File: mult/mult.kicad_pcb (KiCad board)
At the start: 2 copper layers, 20 x 108 mm, 73 parts, among them J1 Eurorack_Mono_Jack, J10 Eurorack_Mono_Jack, J11 Eurorack_Mono_Jack_No_S, J12 Eurorack_Mono_Jack_No_S, J13 Eurorack_Mono_Jack, J14 Eurorack_Mono_Jack, J15 Eurorack_Mono_Jack_No_S, J16 Eurorack_Mono_Jack_No_S, J17 Eurorack_Power, J2 Eurorack_Mono_Jack, J3 Eurorack_Mono_Jack_No_S, J4 Eurorack_Mono_Jack_No_S, J5 Eurorack_Mono_Jack, J6 Eurorack_Mono_Jack, J7 Eurorack_Mono_Jack_No_S, J8 Eurorack_Mono_Jack_No_S, J9 Eurorack_Mono_Jack, U1 OPA1679, U2 OPA1679, U3 OPA1679, U4 OPA1679

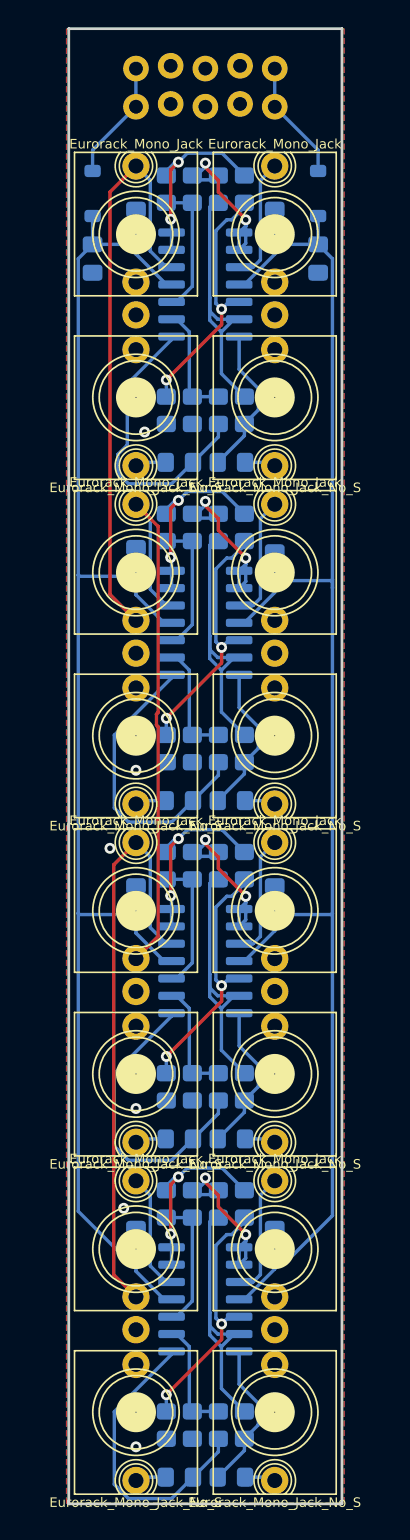
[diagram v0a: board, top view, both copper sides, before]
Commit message: mult: Reassign reference designators
This follows visual placement (left to right, top to bottom), except for
bulk capacitors which are enumerated left to right after bypass caps.
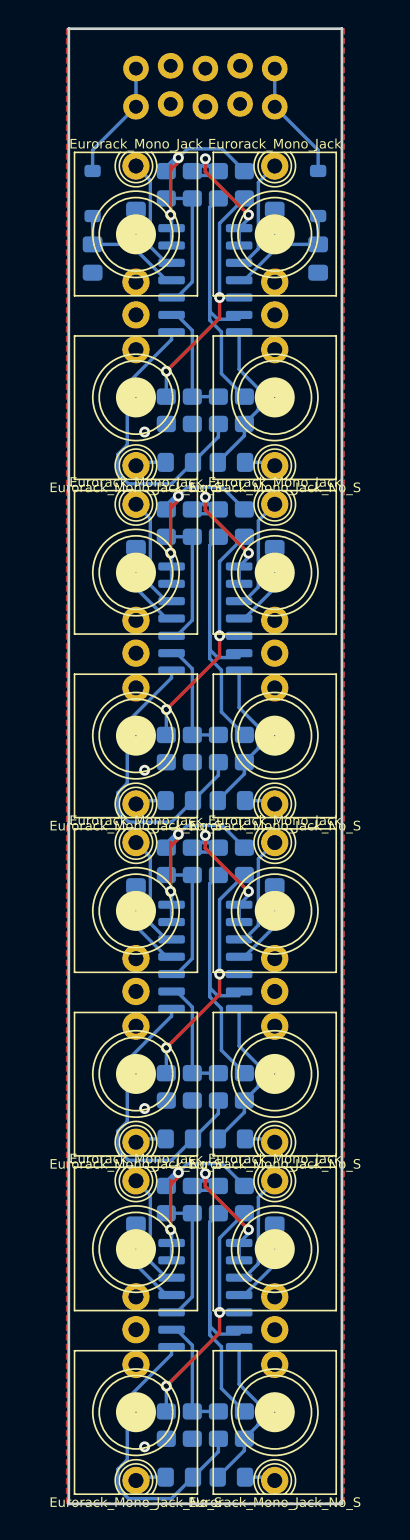
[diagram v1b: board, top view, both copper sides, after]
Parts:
- moved C7 0.32 mm to (15.2, 88.6)
- moved C8 0.32 mm to (5.08, 88.6)
- moved R31 0.32 mm to (13.0, 85.7)
- moved R32 0.32 mm to (11.1, 85.7)
- moved R33 0.32 mm to (9.21, 85.7)
- moved R34 0.32 mm to (7.30, 85.7)
- moved U3 0.32 mm to (10.2, 67.9)
- moved U4 0.32 mm to (10.2, 92.7)
- moved R11 0.32 mm to (13.0, 36.2)
- moved R12 0.32 mm to (11.1, 36.2)
- moved R13 0.32 mm to (9.21, 36.2)
- moved R14 0.32 mm to (7.30, 36.2)
- moved R21 0.32 mm to (13.0, 61.0)
- moved R22 0.32 mm to (11.1, 61.0)
- moved R23 0.32 mm to (9.21, 61.0)
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- renumbered C2 to C1, C9 to C10, C1 to C2, C4 to C3, C3 to C4, C6 to C5, C5 to C6, C8 to C7, C7 to C8, C10 to C9, D2 to D1, D1 to D2, R4 to R1, R5 to R10, R14 to R11, R13 to R12, R12 to R13, R11 to R14, R19 to R15, R17 to R16, R20 to R17, R16 to R19, R3 to R2, R15 to R20, R24 to R21, R23 to R22, R22 to R23, R21 to R24, R29 to R25, R27 to R26, R30 to R27, R26 to R29, R2 to R3, R25 to R30, R34 to R31, R33 to R32, R32 to R33, R31 to R34, R39 to R35, R37 to R36, R40 to R37, R36 to R39, R1 to R4, R35 to R40, R9 to R5, R7 to R6, R10 to R7, R6 to R9
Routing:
- net VEE: track 108.2 -> 21.5 mm
- net VCC: track 107.0 -> 21.5 mm
- net /channel 1/tip in (a): track 43.2 -> 8.01 mm
- net /channel 2/tip in (a): track 43.0 -> 8.01 mm
- net /channel 3/tip in (a): track 42.9 -> 8.01 mm
- net Net-(U2C--): track 14.4 -> 12.5 mm
- net Net-(U3C--): track 14.4 -> 12.5 mm
- net Net-(U1C--): track 14.4 -> 12.5 mm
- net Net-(U4C--): track 14.4 -> 12.5 mm
- net Net-(U4D--): track 20.5 -> 19.2 mm
- net Net-(U3D--): track 20.5 -> 19.2 mm
- net Net-(U1D--): track 20.5 -> 19.2 mm
- net Net-(U2D--): track 20.5 -> 19.2 mm
- net Net-(J10-Tip): track 9.08 -> 8.01 mm
- net Net-(J6-Tip): track 9.08 -> 8.01 mm
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
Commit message: mult: Add 0.5mm power traces
Not sure if this matters at all, but can't hurt.
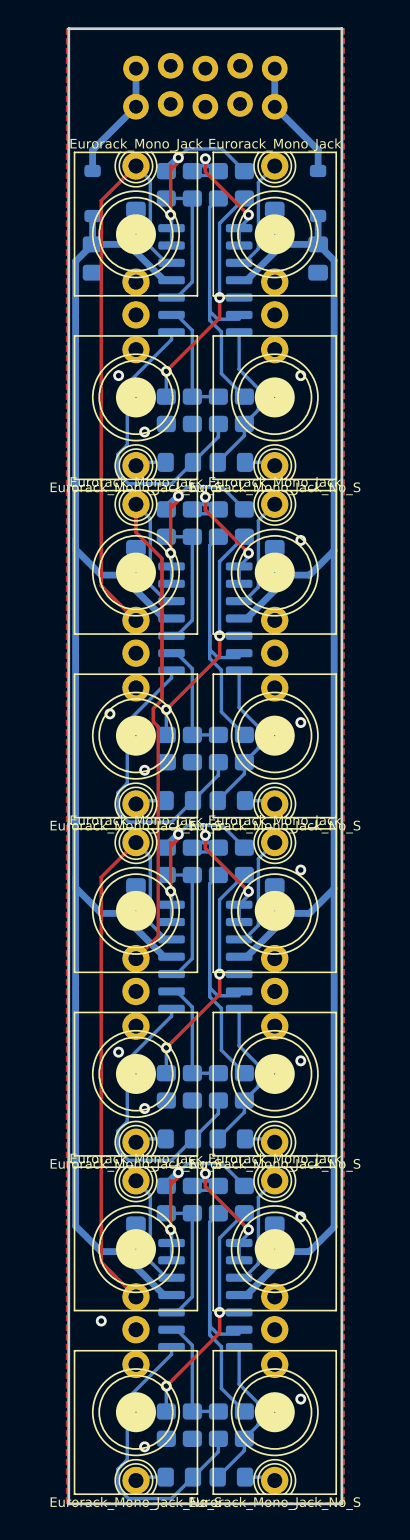
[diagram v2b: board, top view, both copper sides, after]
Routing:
- net VCC: track 21.5 -> 110.2 mm
- net VEE: track 21.5 -> 108.7 mm
- net /channel 3/tip in (a): track 8.01 -> 43.4 mm
- net /channel 1/tip in (a): track 8.01 -> 43.4 mm
- net /channel 2/tip in (a): track 8.01 -> 43.2 mm
- net GND: vias 4 -> 15

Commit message: mult: Initial silkscreen
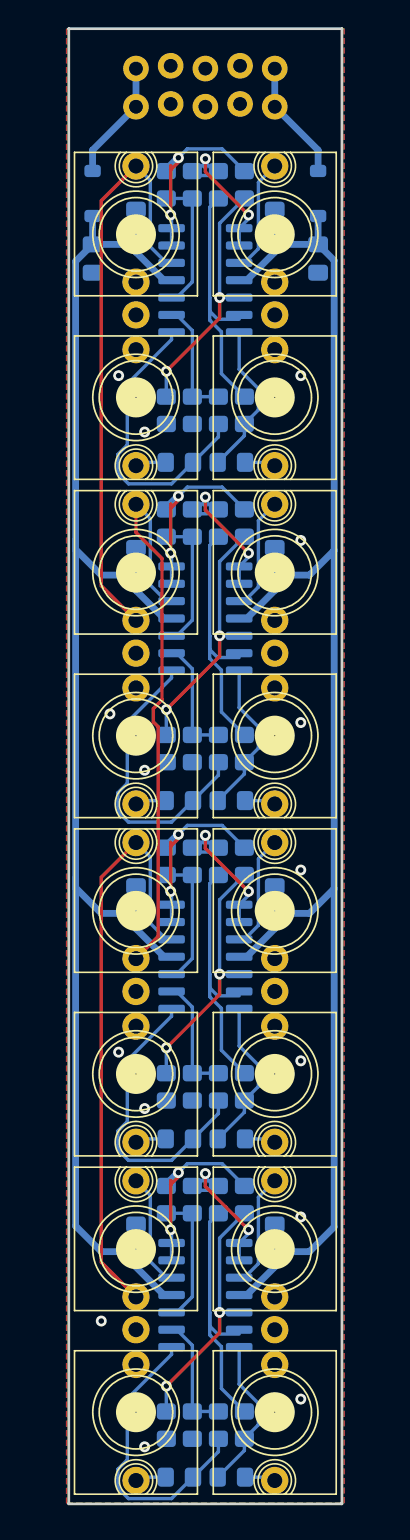
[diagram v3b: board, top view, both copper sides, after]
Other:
- board text added: "R1-4"
- board text added: "R11-14"
- board text added: "R15-18"
- board text added: "R21-24"
- board text added: "R25-28"
- board text added: "R31-34"
- board text added: "R35-38"
- board text added: "R5-8"

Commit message: mult: Not sure what I did, minor PCB changes
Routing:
- net Net-(R36-Pad2): track 21.7 -> 17.4 mm
- net Net-(R26-Pad2): track 21.7 -> 17.5 mm
- net Net-(R10-Pad1): track 21.7 -> 17.6 mm
- net Net-(R16-Pad2): track 21.7 -> 17.6 mm
- net Net-(U2B--): track 13.3 -> 14.2 mm
- net Net-(U3B--): track 13.3 -> 14.2 mm
- net Net-(U1B--): track 13.3 -> 14.2 mm
- net Net-(U4B--): track 13.3 -> 14.2 mm

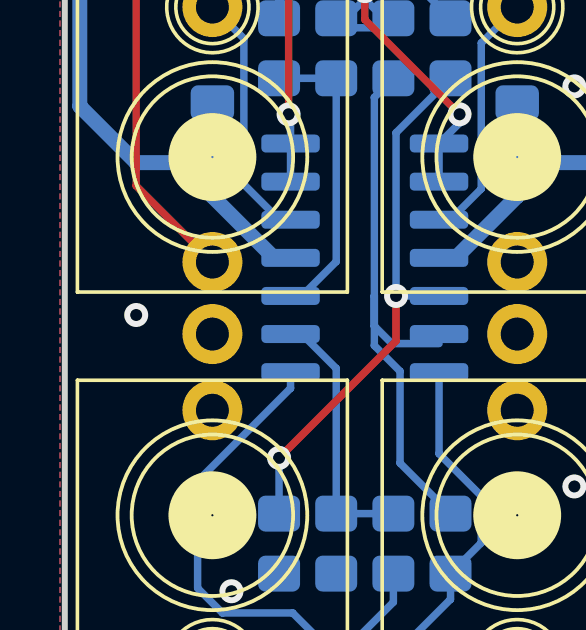
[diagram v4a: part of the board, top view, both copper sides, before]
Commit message: mult: Add components and name to silkscreen
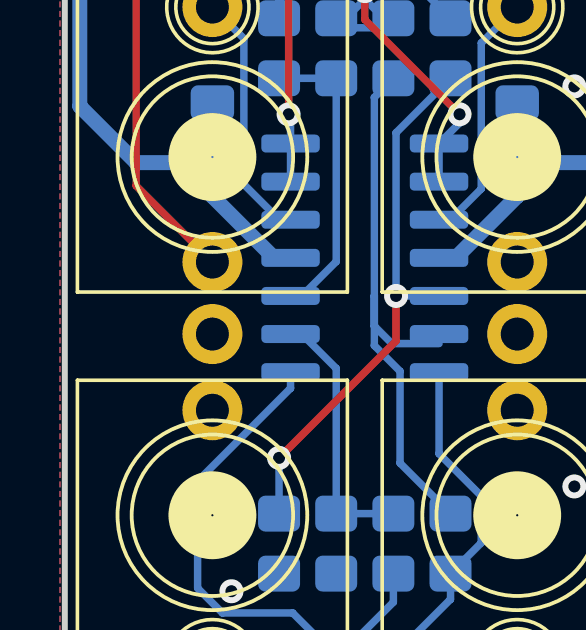
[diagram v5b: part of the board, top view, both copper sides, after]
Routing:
- net GND: vias 15 -> 14
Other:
- board text added: "R1-8: 10k 0.1%, R9-10: 51, C1-8: 100nF, C9-10: 10uF, D1-2: Schottky, U1-4: OPA4991IDR (or substitute) Peter Boström, pineapplemodular.org"
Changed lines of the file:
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@@
     (property "ki_keywords" "cap capacitor")
     (attr smd)
-    (fp_text reference "C10" (at 2.8575 0 90) (layer "B.SilkS")
-        (effects (font (size 0.8 0.8) (thickness 0.15)) (justify mirror))
+    (fp_text reference "C10" (at 1.905 0 90) (layer "B.SilkS")
+        (effects (font (size 0.8 0.8) (thickness 0.15)) (justify left mirror))
     )
     (fp_text value "10uF" (at 0 -1.68 90) (layer "B.Fab")
@@
     (property "ki_keywords" "cap capacitor")
     (attr smd)
-    (fp_text reference "C9" (at 2.54 0 90) (layer "B.SilkS")
-        (effects (font (size 0.8 0.8) (thickness 0.15)) (justify mirror))
+    (fp_text reference "C9" (at 1.905 0 90) (layer "B.SilkS")
+        (effects (font (size 0.8 0.8) (thickness 0.15)) (justify left mirror))
     )
     (fp_text value "10uF" (at 0 -1.68 90) (layer "B.Fab")
@@
   (gr_text "R15-18" (at 13.97 52.705) (layer "B.SilkS")
     (effects (font (size 0.8 0.8) (thickness 0.15)) (justify right mirror))
+  )
+  (gr_text "R1-8: 10k 0.1%, R9-10: 51, C1-8: 100nF, C9-10: 10uF, D1-2: Schottky, U1-4: OPA4991IDR (or substitute)\nPeter Boström, pineapplemodular.org" (at 0.635 107.315 90) (layer "B.SilkS")
+    (effects (font (size 0.8 0.8) (thickness 0.15)) (justify right top mirror))
   )
   (gr_text "R21-24" (at 13.97 61.2775) (layer "B.SilkS")
@@
   (via (at 17.145 25.4) (size 0.8) (drill 0.4) (layers "F.Cu" "B.Cu") (free) (net 2))
   (via (at 3.81 74.93) (size 0.8) (drill 0.4) (layers "F.Cu" "B.Cu") (free) (net 2))
-  (via (at 2.54 94.615) (size 0.8) (drill 0.4) (layers "F.Cu" "B.Cu") (free) (net 2))
   (via (at 17.145 86.995) (size 0.8) (drill 0.4) (layers "F.Cu" "B.Cu") (free) (net 2))
   (via (at 5.715 79.0575) (size 0.8) (drill 0.4) (layers "F.Cu" "B.Cu") (free) (net 2))

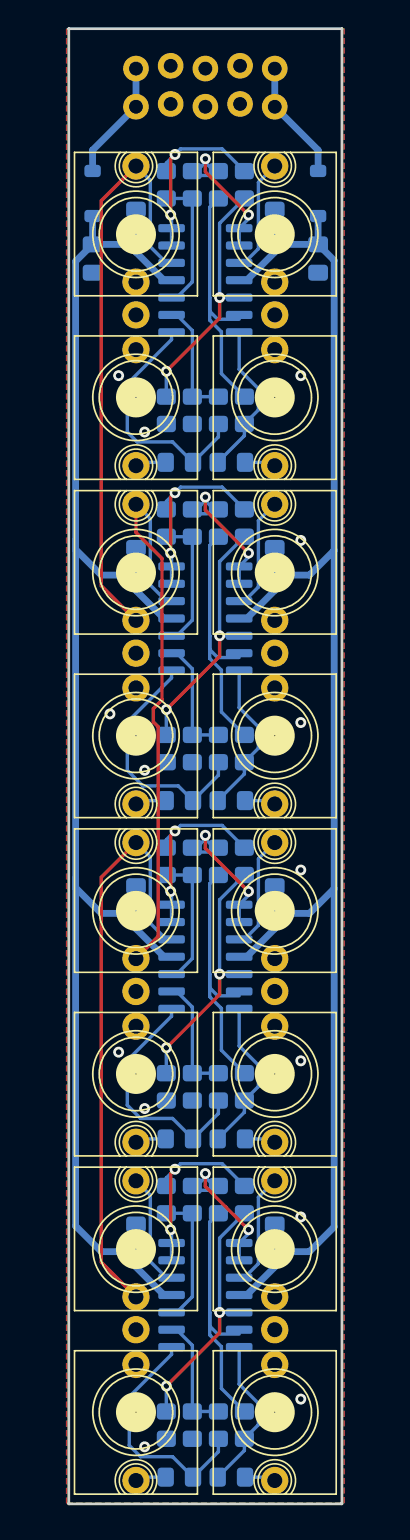
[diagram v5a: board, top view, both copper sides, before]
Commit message: mult: Route power away from board edges
Also drive-by moving power diode and caps so that the D1,D2 text is
visible after parts are placed.
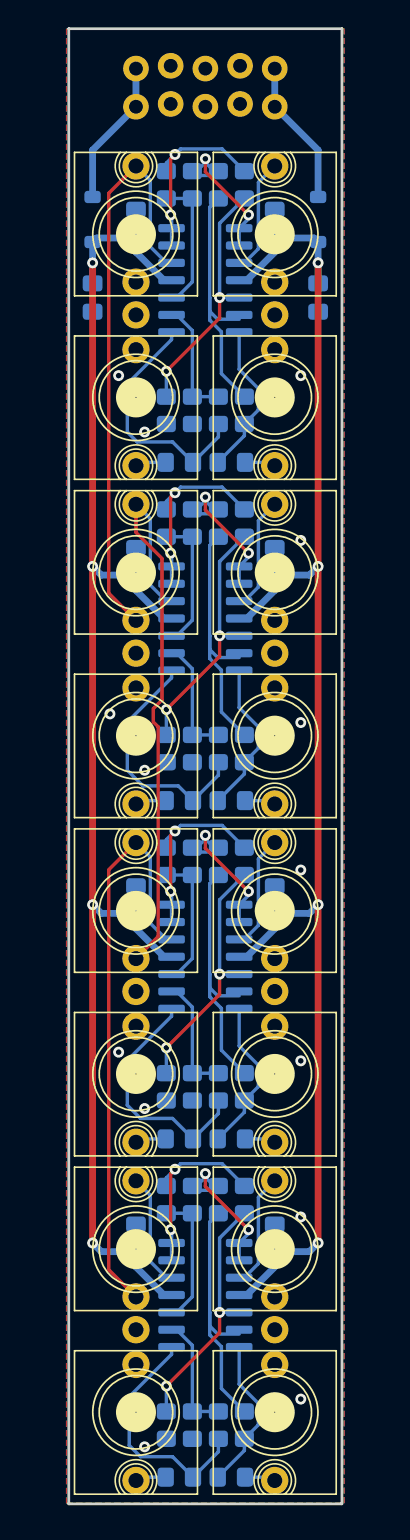
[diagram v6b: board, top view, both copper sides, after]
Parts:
- moved C10 2.86 mm to (1.91, 19.7)
- moved C9 2.86 mm to (18.4, 19.7)
- moved D1 1.91 mm to (18.4, 14.0)
- moved D2 1.91 mm to (1.91, 14.0)
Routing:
- net VCC: track 110.2 -> 103.9 mm, vias 0 -> 4
- net VEE: track 108.7 -> 103.9 mm, vias 0 -> 4
- net Net-(D2-A): track 8.81 -> 10.7 mm
- net Net-(D1-K): track 8.81 -> 10.7 mm
